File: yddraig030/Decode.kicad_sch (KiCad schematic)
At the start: 12 parts, among them J1501 JTAG, U1502 74LS04, U1503 74LS21, U1504 74HC164, U1505 74LS138, U1506 74LS541, U1508 74LS07, X1501 40Mhz

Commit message: More changes to the 030 board
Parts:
- removed RN1503: 10K, Resistor_THT:R_Array_SIP9, symbol Device:R_Network08
- added C? (x8): 100nF, symbol Device:C
- added R? (x2): 10K, symbol Device:R
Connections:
- net +5V: now also C?.1, C?.1, C?.1, C?.1, C?.1, C?.1, C?.1, C?.1, R?.1, R?.1
- net GND: now also C?.2, C?.2, C?.2, C?.2, C?.2, C?.2, C?.2, C?.2
- net ~{DSACK0}: now also R?.2
- net ~{DSACK1}: now also R?.2
- net ~{CS_INTERRUPT}: now reaches U?.74 (I/O/GSR)
- net ~{CDIS}: no longer names the net of U?.36 (P36)
- net ~{MMUDIS}: no longer names the net of U?.35 (P35)
- no-connect marks 20 -> 14
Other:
- moved on the sheet: U1502G, U1503A, U1503B, U1503C, U1508A, U1508B

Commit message: ddraig030 schematic done
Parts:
- added U708: 74LS541, Package_DIP:DIP-20_W7.62mm_Socket, symbol 74xx:74LS541
- gave numbers to parts that had none: 11
- renumbered J1501 to J701, R1501 to R701, RN1502 to RN701, U1508 to U701, U1502 to U702, U1504 to U704, U1503 to U705, U1505 to U706, U1506 to U707, X1501 to X701
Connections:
- net RD/~{WR} is gone; now on net R/~{W}: U702.9
- net +5V: now also U708.20 (VCC)
- net D24: now also U708.18 (Y0)
- net D25: now also U708.17 (Y1)
- net D26: now also U708.16 (Y2)
- net D27: now also U708.15 (Y3)
- net D28: now also U708.14 (Y4)
- net D29: now also U708.13 (Y5)
- net D30: now also U708.12 (Y6)
- net D31: now also U708.11 (Y7)
- net GND: now also U708.10 (GND), U708.19 (G2)
- net ~{CIIN}: now also U703.72 (P72)
- net ~{FPUSENSE}: now also U708.2 (A0); no longer U703.83 (P83)
- net ~{CS_DRAMPD}: now reaches U703.35 (P35)
- net ~{CS_PIT}: now reaches U703.36 (P36)
- net ~{VMA}: now reaches U703.37 (P37)
- net R/~{W}: now reaches U703.40 (P40)
- net ~{CS_STATUS}: now reaches U703.41 (P41)
- net ~{CS_STATUS}: now also U708.1 (G1)
- net ~{IPEND}: now reaches U703.57 (P57)
- net ~{AVEC}: now reaches U703.71 (P71)
- net ~{RD}/WR renamed ~{R}/W
- new net ~{CDIS}: U708.3 (A1)
- new net ~{MMUDIS}: U708.4 (A2)
- no-connect marks 14 -> 19
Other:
- moved on the sheet: J701, R702, R703, RN701, U701A, U701B, U702A, U702D, U703, U705A, U705B, U706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

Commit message: Small changes to 030 design
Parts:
- C701, C702, C703, C704, C705, C706, C707, C708: footprint (none) -> Capacitor_THT:C_Disc_D3.8mm_W2.6mm_P2.50mm
- R702, R703: footprint (none) -> Resistor_THT:R_Axial_DIN0207_L6.3mm_D2.5mm_P10.16mm_Horizontal
- U701: footprint (none) -> Package_DIP:DIP-14_W7.62mm_Socket
- U703: footprint (none) -> Package_LCC:PLCC-84_THT-Socket
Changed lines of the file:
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@@
     (property "Reference" "U701" (id 0) (at 266.7 214.7062 0))
     (property "Value" "74LS07" (id 1) (at 266.7 217.0176 0))
-    (property "Footprint" "" (id 2) (at 266.7 222.758 0)
+    (property "Footprint" "Package_DIP:DIP-14_W7.62mm_Socket" (id 2) (at 266.7 222.758 0)
       (effects (font (size 1.27 1.27)) hide)
     )
@@
     (property "Reference" "U701" (id 0) (at 266.7 228.6762 0))
     (property "Value" "74LS07" (id 1) (at 266.7 230.9876 0))
-    (property "Footprint" "" (id 2) (at 266.7 236.728 0)
+    (property "Footprint" "Package_DIP:DIP-14_W7.62mm_Socket" (id 2) (at 266.7 236.728 0)
       (effects (font (size 1.27 1.27)) hide)
     )
@@
     (property "Reference" "U701" (id 0) (at 39.37 216.1032 0))
     (property "Value" "74LS07" (id 1) (at 39.37 218.4146 0))
-    (property "Footprint" "" (id 2) (at 39.37 224.155 0)
+    (property "Footprint" "Package_DIP:DIP-14_W7.62mm_Socket" (id 2) (at 39.37 224.155 0)
       (effects (font (size 1.27 1.27)) hide)
     )
@@
     (property "Reference" "U701" (id 0) (at 39.37 228.8032 0))
     (property "Value" "74LS07" (id 1) (at 39.37 231.1146 0))
-    (property "Footprint" "" (id 2) (at 39.37 236.855 0)
+    (property "Footprint" "Package_DIP:DIP-14_W7.62mm_Socket" (id 2) (at 39.37 236.855 0)
       (effects (font (size 1.27 1.27)) hide)
     )
@@
     (property "Reference" "U701" (id 0) (at 39.37 241.5032 0))
     (property "Value" "74LS07" (id 1) (at 39.37 243.8146 0))
-    (property "Footprint" "" (id 2) (at 39.37 249.555 0)
+    (property "Footprint" "Package_DIP:DIP-14_W7.62mm_Socket" (id 2) (at 39.37 249.555 0)
       (effects (font (size 1.27 1.27)) hide)
     )
@@
     (property "Reference" "U701" (id 0) (at 39.37 254.2032 0))
     (property "Value" "74LS07" (id 1) (at 39.37 256.5146 0))
-    (property "Footprint" "" (id 2) (at 39.37 262.255 0)
+    (property "Footprint" "Package_DIP:DIP-14_W7.62mm_Socket" (id 2) (at 39.37 262.255 0)
       (effects (font (size 1.27 1.27)) hide)
     )
@@
       (effects (font (size 1.27 1.27)) (justify left))
     )
-    (property "Footprint" "" (id 2) (at 352.425 223.52 0)
+    (property "Footprint" "Package_DIP:DIP-14_W7.62mm_Socket" (id 2) (at 352.425 223.52 0)
       (effects (font (size 1.27 1.27)) hide)
     )
@@
       (effects (font (size 1.27 1.27)) (justify left))
     )
-    (property "Footprint" "" (id 2) (at 158.5722 266.573 0)
+    (property "Footprint" "Capacitor_THT:C_Disc_D3.8mm_W2.6mm_P2.50mm" (id 2) (at 158.5722 266.573 0)
       (effects (font (size 1.27 1.27)) hide)
     )
@@
       (effects (font (size 1.27 1.27)) (justify left))
     )
-    (property "Footprint" "" (id 2) (at 146.5072 266.573 0)
+    (property "Footprint" "Capacitor_THT:C_Disc_D3.8mm_W2.6mm_P2.50mm" (id 2) (at 146.5072 266.573 0)
       (effects (font (size 1.27 1.27)) hide)
     )
@@
       (effects (font (size 1.27 1.27)) (justify left))
     )
-    (property "Footprint" "" (id 2) (at 170.6372 266.573 0)
+    (property "Footprint" "Capacitor_THT:C_Disc_D3.8mm_W2.6mm_P2.50mm" (id 2) (at 170.6372 266.573 0)
       (effects (font (size 1.27 1.27)) hide)
     )
@@
       (effects (font (size 1.27 1.27)) (justify left))
     )
-    (property "Footprint" "" (id 2) (at 221.1832 266.573 0)
+    (property "Footprint" "Capacitor_THT:C_Disc_D3.8mm_W2.6mm_P2.50mm" (id 2) (at 221.1832 266.573 0)
       (effects (font (size 1.27 1.27)) hide)
     )
@@
       (effects (font (size 1.27 1.27)) (justify left))
     )
-    (property "Footprint" "" (id 2) (at 197.0532 266.573 0)
+    (property "Footprint" "Capacitor_THT:C_Disc_D3.8mm_W2.6mm_P2.50mm" (id 2) (at 197.0532 266.573 0)
       (effects (font (size 1.27 1.27)) hide)
     )
@@
       (effects (font (size 1.27 1.27)) (justify left))
     )
-    (property "Footprint" "" (id 2) (at 209.1182 266.573 0)
+    (property "Footprint" "Capacitor_THT:C_Disc_D3.8mm_W2.6mm_P2.50mm" (id 2) (at 209.1182 266.573 0)
       (effects (font (size 1.27 1.27)) hide)
     )
@@
       (effects (font (size 1.27 1.27)) (justify left))
     )
-    (property "Footprint" "" (id 2) (at 233.2482 266.573 0)
+    (property "Footprint" "Capacitor_THT:C_Disc_D3.8mm_W2.6mm_P2.50mm" (id 2) (at 233.2482 266.573 0)
       (effects (font (size 1.27 1.27)) hide)
     )
@@
       (effects (font (size 1.27 1.27)) (justify left))
     )
-    (property "Footprint" "" (id 2) (at 109.22 106.68 0)
+    (property "Footprint" "Package_LCC:PLCC-84_THT-Socket" (id 2) (at 109.22 106.68 0)
       (effects (font (size 1.27 1.27)) hide)
     )
@@
       (effects (font (size 1.27 1.27)) (justify left))
     )
-    (property "Footprint" "" (id 2) (at 276.352 208.534 90)
+    (property "Footprint" "Resistor_THT:R_Axial_DIN0207_L6.3mm_D2.5mm_P10.16mm_Horizontal" (id 2) (at 276.352 208.534 90)
       (effects (font (size 1.27 1.27)) hide)
     )
@@
       (effects (font (size 1.27 1.27)) (justify left))
     )
-    (property "Footprint" "" (id 2) (at 286.258 208.534 90)
+    (property "Footprint" "Resistor_THT:R_Axial_DIN0207_L6.3mm_D2.5mm_P10.16mm_Horizontal" (id 2) (at 286.258 208.534 90)
       (effects (font (size 1.27 1.27)) hide)
     )
@@
       (effects (font (size 1.27 1.27)) (justify left))
     )
-    (property "Footprint" "" (id 2) (at 182.7022 266.573 0)
-      (effects (font (size 1.27 1.27)) hide)
-    )
+    (property "Footprint" "Capacitor_THT:C_Disc_D3.8mm_W2.6mm_P2.50mm" (id 2) (at 182.7022 266.573 0)
+      (effects (font (size 1.27 1.27)) hide)
+    )

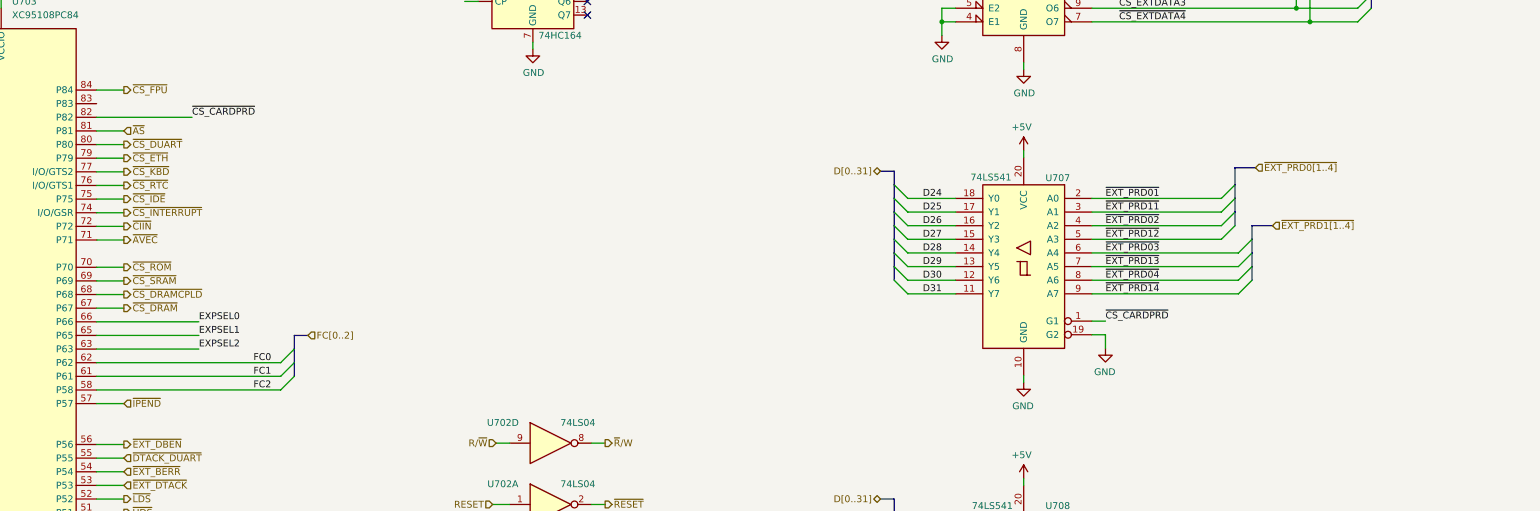
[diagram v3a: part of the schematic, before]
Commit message: yddraig030: Fixed ERC check errors
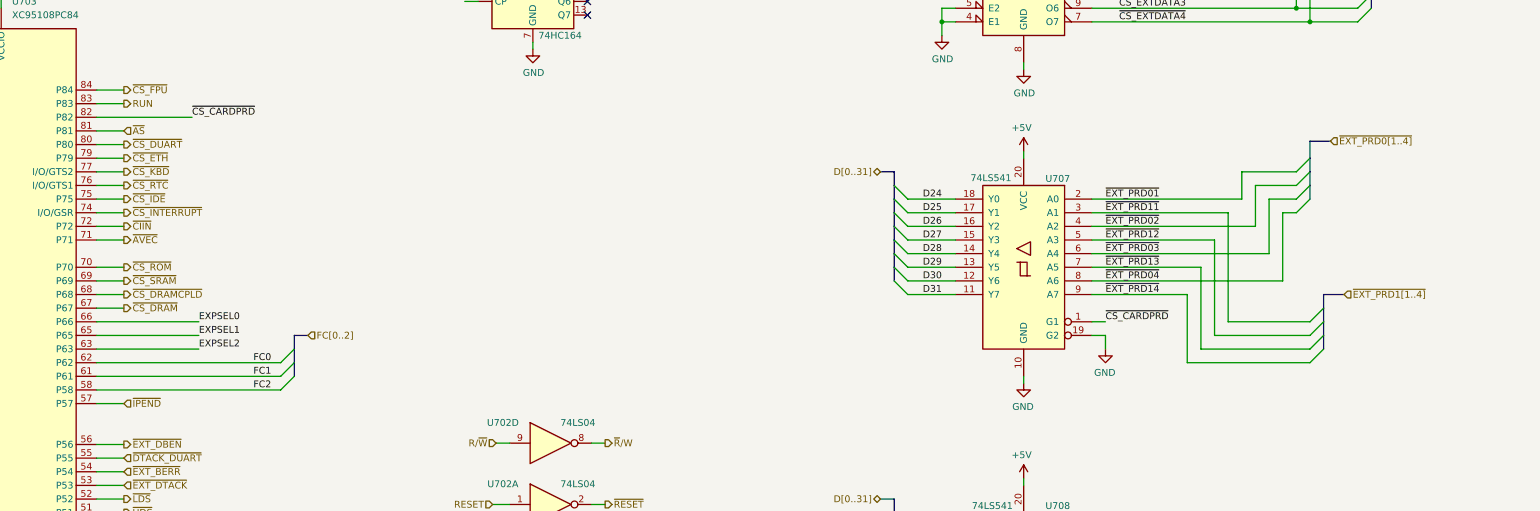
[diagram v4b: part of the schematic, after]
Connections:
- net RUN: now reaches U703.83 (P83)

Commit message: Started PCB layout
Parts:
- added unit 2 of U702
- U705: footprint Package_DIP:DIP-12_W7.62mm_Socket -> Package_DIP:DIP-14_W7.62mm_Socket
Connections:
- net +5V: now also U702.1, U702.3; no longer U702.11, U702.13
- net RESET: now also U702.11; no longer U702.1
- net ~{RESET}: now also U702.10; no longer U702.2
- net ~{INT_ETH}: now reaches U702.12
- new net INT_ETH: U702.13

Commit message: yddraig030: board changed, ready for footprint assignment
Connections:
- net ~{CS_DRAMCPLD}: no longer names the net of U703.68 (P68)
- net ~{CS_DRAMPD}: no longer names the net of U703.35 (P35)
- net ~{CS_PIT}: no longer names the net of U703.36 (P36)
- net ~{DTACK_PIT}: no longer names the net of U703.50 (P50)
- no-connect marks 19 -> 23
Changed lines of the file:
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@@
   (no_connect (at 107.95 227.33))
   (no_connect (at 223.52 49.53))
+  (no_connect (at 132.08 147.32))
+  (no_connect (at 86.36 144.78))
+  (no_connect (at 86.36 142.24))
+  (no_connect (at 132.08 104.14))
   (no_connect (at 46.99 224.155))
   (no_connect (at 223.52 52.07))
@@
     (stroke (width 0) (type default) (color 0 0 0 0))
   )
-  (wire (pts (xy 63.5 144.78) (xy 86.36 144.78))
-    (stroke (width 0) (type default) (color 0 0 0 0))
-  )
   (bus (pts (xy 280.67 142.24) (xy 280.67 144.78))
     (stroke (width 0) (type default) (color 0 0 0 0))
@@
     (stroke (width 0) (type default) (color 0 0 0 0))
   )
-  (wire (pts (xy 137.16 104.14) (xy 132.08 104.14))
-    (stroke (width 0) (type default) (color 0 0 0 0))
-  )
   (bus (pts (xy 280.67 88.9) (xy 280.67 91.44))
     (stroke (width 0) (type default) (color 0 0 0 0))
@@
     (stroke (width 0) (type default) (color 0 0 0 0))
   )
-  (wire (pts (xy 63.5 142.24) (xy 86.36 142.24))
-    (stroke (width 0) (type default) (color 0 0 0 0))
-  )
   (bus (pts (xy 369.57 48.26) (xy 369.57 50.8))
     (stroke (width 0) (type default) (color 0 0 0 0))
@@
     (stroke (width 0) (type default) (color 0 0 0 0))
   )
-  (wire (pts (xy 132.08 147.32) (xy 137.16 147.32))
-    (stroke (width 0) (type default) (color 0 0 0 0))
-  )
   (wire (pts (xy 274.32 236.728) (xy 288.036 236.728))
     (stroke (width 0) (type default) (color 0 0 0 0))
@@
   )
   (hierarchical_label "~{CDIS}" (shape input) (at 322.58 149.86 0)
-    (effects (font (size 1.27 1.27)) (justify left))
-  )
-  (hierarchical_label "~{DTACK_PIT}" (shape input) (at 137.16 147.32 0)
     (effects (font (size 1.27 1.27)) (justify left))
   )
@@
     (effects (font (size 1.27 1.27)) (justify left))
   )
-  (hierarchical_label "~{CS_PIT}" (shape output) (at 63.5 144.78 180)
-    (effects (font (size 1.27 1.27)) (justify right))
-  )
   (hierarchical_label "~{CS_IDE}" (shape output) (at 137.16 86.36 0)
     (effects (font (size 1.27 1.27)) (justify left))
@@
     (effects (font (size 1.27 1.27)) (justify left))
   )
-  (hierarchical_label "~{CS_DRAMCPLD}" (shape output) (at 137.16 104.14 0)
-    (effects (font (size 1.27 1.27)) (justify left))
-  )
   (hierarchical_label "~{AVEC}" (shape output) (at 137.16 93.98 0)
     (effects (font (size 1.27 1.27)) (justify left))
@@
     (effects (font (size 1.27 1.27)) (justify left))
   )
-  (hierarchical_label "~{CS_DRAMPD}" (shape output) (at 63.5 142.24 180)
-    (effects (font (size 1.27 1.27)) (justify right))
-  )
   (hierarchical_label "D[0..31]" (shape bidirectional) (at 278.13 142.24 180)

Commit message: Working on PCB layout
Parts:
- C701, C702, C703, C704, C705, C706, C707, C708: footprint Capacitor_THT:C_Disc_D3.8mm_W2.6mm_P2.50mm -> Capacitor_SMD:C_0805_2012Metric
- R701, R702, R703: footprint Resistor_THT:R_Axial_DIN0207_L6.3mm_D2.5mm_P10.16mm_Horizontal -> Resistor_SMD:R_0805_2012Metric
- U701, U702, U704, U705: footprint Package_DIP:DIP-14_W7.62mm_Socket -> Package_SO:SO-14_3.9x8.65mm_P1.27mm
- U706: footprint Package_DIP:DIP-16_W7.62mm_Socket -> Package_SO:SO-16_3.9x9.9mm_P1.27mm
- U707, U708: footprint Package_DIP:DIP-20_W7.62mm_Socket -> Package_SO:SO-20_5.3x12.6mm_P1.27mm
